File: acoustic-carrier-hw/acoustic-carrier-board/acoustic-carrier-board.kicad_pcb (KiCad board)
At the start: 6 copper layers, 78.8 x 95 mm, 361 parts, among them IC1 ECP5-BGA256, IC1101 MT41K256M16TW-107_P, J1001 BWU.FL-IPEX1, J1002 BWU.FL-IPEX1, J1003 BWU.FL-IPEX1, J1004 BWU.FL-IPEX1, J1005 BWU.FL-IPEX1, J1006 BWU.FL-IPEX1, J1007 8P8C_Shielded, J1008 BWU.FL-IPEX1, J1009 BWU.FL-IPEX1, J1010 BWU.FL-IPEX1, J1201 HR911130A, J202 Conn_02x04_Odd_Even, J701 Conn_01x10_Socket, J702 Conn_01x08_Socket, J801 TYPE-C-31-M-12, J901 Conn_02x08_Odd_Even, Q201 AO3401A, U1001 MS9280, U1002 THS4521IDGK, U1003 DGQ2788AEN-T1-GE4, U1004 LMV321, U1005 TL432DBZ, U1201 KSZ9031RN, U201 TPS2121RUX, U202 TLV62569DBV, U203 TLV62569DBV, U204 TLV62569DBV, U205 TLV62569DBV, U206 OPA376xxDBV, U701 W25Q128JVS, U702 W25Q128JVS, U801 USB3300-EZK, U802 LMV321, Y1201 25MHz, Y401 Crystal Oscillator, Y801 Crystal_GND24_Small

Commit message: [carrier] Layout more or less complete (next) think about adding 6x2 connectors, and add extra pin signals to the connector for testing
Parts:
- removed J1004: BWU.FL-IPEX1, iw-connector:BWU.FL-IPEX1
- removed J202: Conn_02x04_Odd_Even, Connector_PinSocket_2.54mm:PinSocket_2x04_P2.54mm_Horizontal
- removed J702: Conn_01x08_Socket, Connector_PinSocket_2.54mm:PinSocket_1x08_P2.54mm_Horizontal
- removed J901: Conn_02x08_Odd_Even, Connector_PinSocket_2.54mm:PinSocket_2x08_P2.54mm_Horizontal
- removed TP1008: TestPoint, TestPoint:TestPoint_Pad_1.0x1.0mm
- added J201: Conn_02x05_Odd_Even, Connector_PinSocket_2.54mm:PinSocket_2x05_P2.54mm_Horizontal, F.Cu at (115.2, 56.6)
- added J703: Conn_02x05_Odd_Even, Connector_PinSocket_2.54mm:PinSocket_2x05_P2.54mm_Horizontal, F.Cu at (51.3, 103.9)
- added J902: Conn_02x05_Odd_Even, Connector_PinSocket_2.54mm:PinSocket_2x05_P2.54mm_Horizontal, F.Cu at (50.2, 60.9)
- added R1008: 0, Resistor_SMD:R_0603_1608Metric, F.Cu at (66.8, 133.0)
- added R1043: 0, Resistor_SMD:R_0603_1608Metric, F.Cu at (66.8, 138.5)
- C1229, C301, C302, C303, C304, C305, C306, C307, C308, C309, C407, D1201, R1001, R1002, R1003, R1004, R1005, R1025, R1203, R1204, R1206, R1207, R1208, R1209, R1210, R1211, R1212, R1213, R401, R701, R702, R703, RN1201, RN701, RN702, U701, U702: moved to B.Cu
- J1003, J1005: moved to F.Cu
- J701: value Conn_01x10_Socket -> Conn_02x05_Odd_Even; footprint Connector_PinSocket_2.54mm:PinSocket_1x10_P2.54mm_Horizontal -> Connector_PinSocket_2.54mm:PinSocket_2x05_P2.54mm_Horizontal
- R1205: footprint Resistor_SMD:R_0805_2012Metric_Pad1.20x1.40mm_HandSolder -> Resistor_SMD:R_0402_1005Metric; moved to B.Cu
- TP1005: footprint TestPoint:TestPoint_Loop_D1.80mm_Drill1.0mm_Beaded -> TestPoint:TestPoint_THTPad_1.5x1.5mm_Drill0.7mm
- moved TP205 262.9 mm to (-88.4, 99.6)
- moved TP207 262.9 mm to (-89.0, 95.0)
- moved RN701 262.6 mm to (113.2, 107.5), turned to 0 degrees
- moved R701 262.0 mm to (112.7, 116.4), turned to 180 degrees
- moved R702 261.0 mm to (112.7, 115.3), turned to 180 degrees
- moved R703 260.0 mm to (112.7, 114.3), turned to 0 degrees
- moved RN702 258.6 mm to (113.0, 111.5), turned to 180 degrees
- moved TP210 255.9 mm to (-85.2, 105.3)
- moved TP807 255.9 mm to (-93.2, 104.8)
- moved TP801 255.9 mm to (-81.0, 101.5)
- moved TP804 255.9 mm to (-83.7, 94.1)
- moved J701 236.1 mm to (120.1, 112.8), turned to 180 degrees
- moved TP1011 233.0 mm to (-25.4, 94.9)
- moved TP1012 221.8 mm to (-25.8, 100.3), turned to 0 degrees
- moved RN1201 218.5 mm to (77.5, 86.8), turned to 180 degrees
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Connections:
- C1019 pad 1: VCORE_3V3 -> VDDA
- J1007 pad 4: Net-(C1018-Pad1) -> unconnected-(J1007-Pad4)
- J1007 pad 5: Net-(C1017-Pad1) -> unconnected-(J1007-Pad5)
- J1007 pad 7: unconnected-(J1007-Pad7) -> Net-(C1018-Pad1)
- J1007 pad 8: unconnected-(J1007-Pad8) -> Net-(C1017-Pad1)
- J701 pad 10: /FPGA-CONFIG-FLASH/FPGA_RESET -> /FPGA-CONFIG-FLASH/FPGA_CFG1
- J701 pad 2: /FPGA-CONFIG-FLASH/JTAG.TCK -> /FPGA-CONFIG-FLASH/FPGA_RESET
- J701 pad 3: /FPGA-CONFIG-FLASH/JTAG.TDI -> /FPGA-CONFIG-FLASH/JTAG.TCK
- J701 pad 4: /FPGA-CONFIG-FLASH/JTAG.TDO -> /FPGA-CONFIG-FLASH/~{FPGA_INIT}
- J701 pad 5: /FPGA-CONFIG-FLASH/FPGA_CFG0 -> /FPGA-CONFIG-FLASH/JTAG.TDI
- J701 pad 6: /FPGA-CONFIG-FLASH/FPGA_CFG1 -> /FPGA-CONFIG-FLASH/FPGA_DONE
- J701 pad 7: /FPGA-CONFIG-FLASH/FPGA_CFG2 -> /FPGA-CONFIG-FLASH/JTAG.TDO
- J701 pad 8: /FPGA-CONFIG-FLASH/FPGA_DONE -> /FPGA-CONFIG-FLASH/FPGA_CFG2
- J701 pad 9: /FPGA-CONFIG-FLASH/~{FPGA_INIT} -> /FPGA-CONFIG-FLASH/FPGA_CFG0
- RJ1001 pad 1: Net-(J1009-In) -> /ANALOG-FRONTEND/MAG_ADC_AIN-
- RJ1001 pad 2: Net-(J1010-In) -> /ANALOG-FRONTEND/MAG_ADC_AIN+
- RJ1001 pad 3: /ANALOG-FRONTEND/MAG_ADC_AIN- -> Net-(J1009-In)
- RJ1001 pad 4: GND -> Net-(R1039-Pad2)
- RJ1001 pad 5: Net-(R1039-Pad2) -> GND
- RJ1001 pad 6: /ANALOG-FRONTEND/MAG_ADC_AIN+ -> Net-(J1010-In)
- U1003 pad 3: Net-(J1004-In) -> unconnected-(U1003-NO3-Pad3)
- U1003 pad 4: Net-(J1005-In) -> unconnected-(U1003-COM3-Pad4)
- U1003 pad 5: Net-(J1003-In) -> unconnected-(U1003-NC3-Pad5)
- U1003 pad 6: Net-(U1003-IN3-4) -> unconnected-(U1003-IN3-4-Pad6)
- U1004 pad 5: VCORE_3V3 -> VDDA

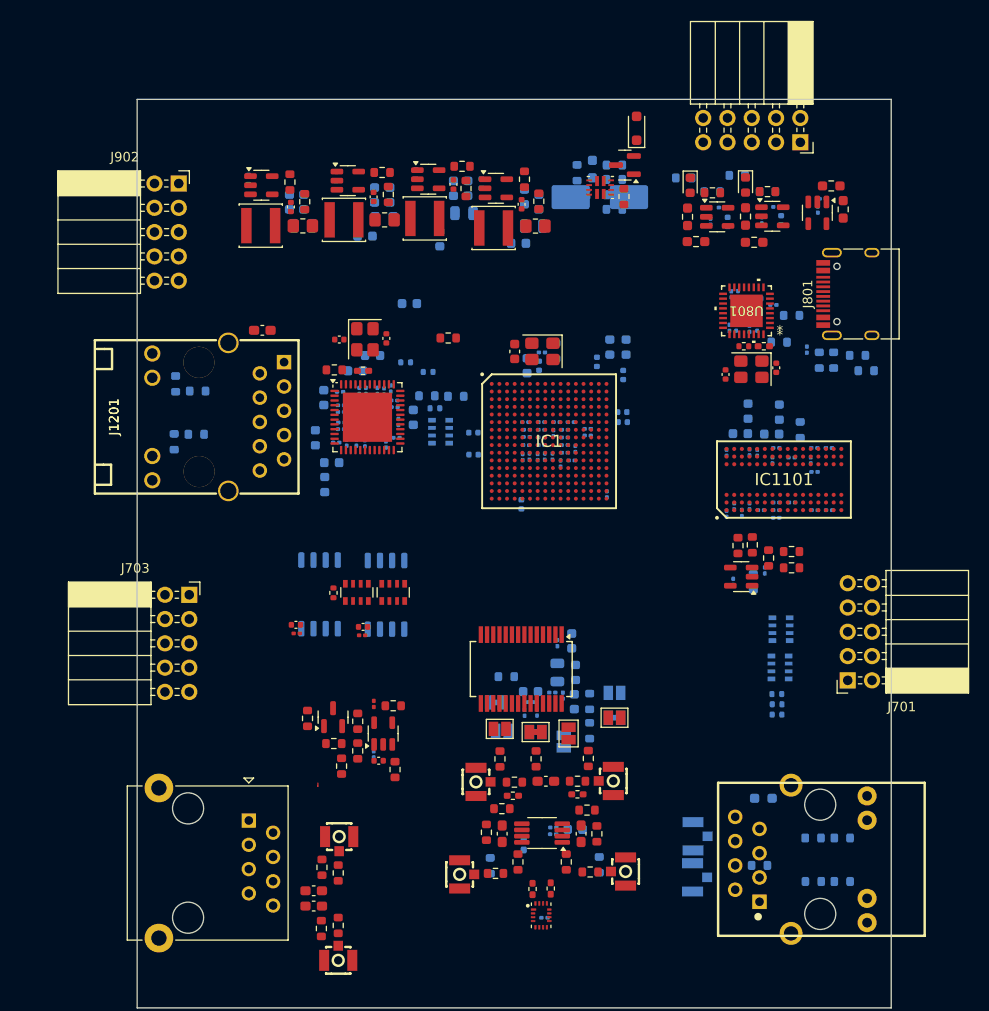
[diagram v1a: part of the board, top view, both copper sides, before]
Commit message: [carrier] Added testpoints to rj45, added 6xx2 connectors (next) start routing the digital section
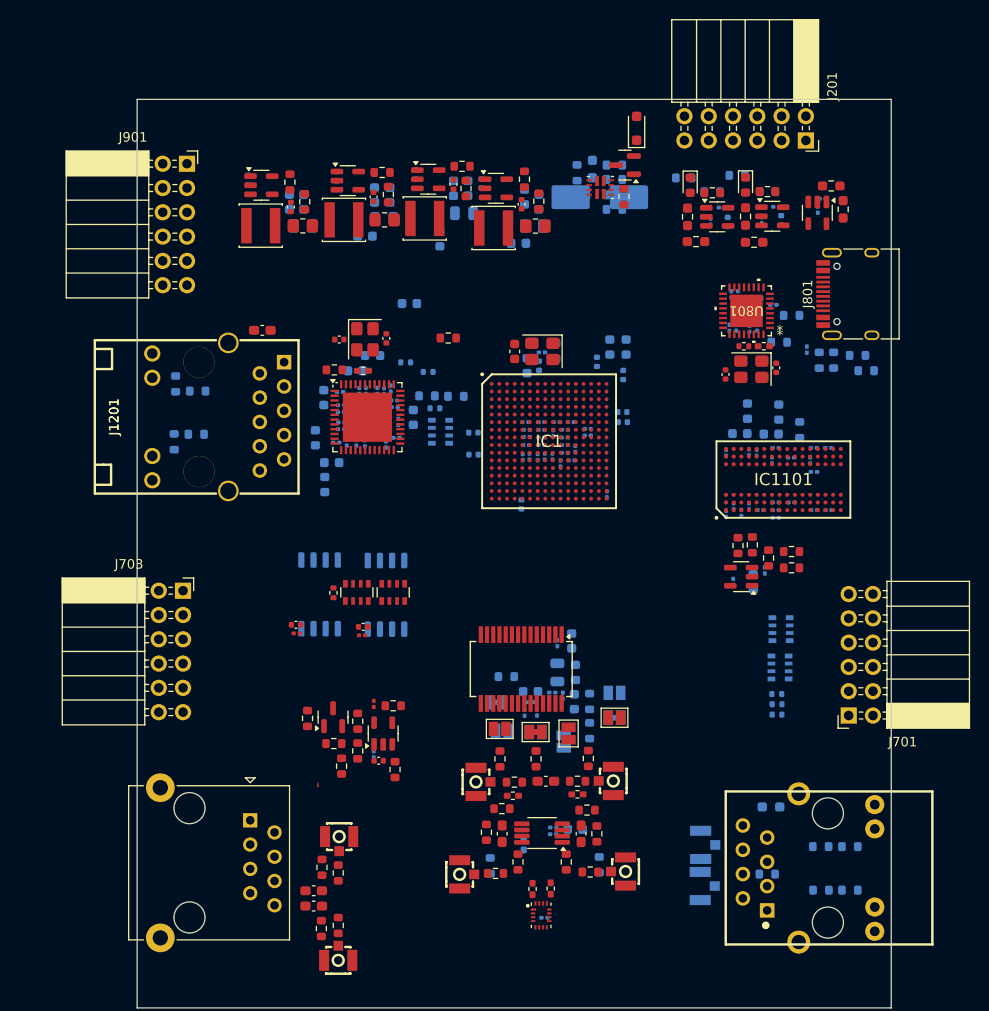
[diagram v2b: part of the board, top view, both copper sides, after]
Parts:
- removed J902: Conn_02x05_Odd_Even, Connector_PinSocket_2.54mm:PinSocket_2x05_P2.54mm_Horizontal
- added J901: Conn_02x06_Odd_Even, Connector_PinSocket_2.54mm:PinSocket_2x06_P2.54mm_Horizontal, F.Cu at (51.0, 58.8)
- J201, J701, J703: value Conn_02x05_Odd_Even -> Conn_02x06_Odd_Even; footprint Connector_PinSocket_2.54mm:PinSocket_2x05_P2.54mm_Horizontal -> Connector_PinSocket_2.54mm:PinSocket_2x06_P2.54mm_Horizontal
- moved J701 3.68 mm to (120.2, 116.5)
- moved J1009 1.21 mm to (105.5, 134.4)
- moved R1001 1.21 mm to (112.1, 126.1)
- moved R1002 1.21 mm to (120.4, 130.2)
- moved R1004 1.21 mm to (120.4, 134.8)
- moved J1010 1.21 mm to (105.5, 130.1)
- moved R1003 1.21 mm to (117.3, 130.2)
- moved R1005 1.21 mm to (117.3, 134.8)
- moved R1039 1.21 mm to (111.7, 133.1)
- moved RJ1001 1.21 mm to (116.1, 132.5)
- moved J703 0.78 mm to (50.6, 103.5)
- moved J201 0.61 mm to (115.8, 56.4)
- moved J1007 0.15 mm to (57.6, 127.5)
- moved C1102 0.06 mm to (111.0, 95.0)
- moved C1105 0.06 mm to (118.1, 88.5)
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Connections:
- J701 pad 1: /FPGA-CONFIG-FLASH/JTAG.TMS -> unconnected-(J701-Pin_1-Pad1)
- J701 pad 10: /FPGA-CONFIG-FLASH/FPGA_CFG1 -> /FPGA-CONFIG-FLASH/JTAG.TDO
- J701 pad 2: /FPGA-CONFIG-FLASH/FPGA_RESET -> unconnected-(J701-Pin_2-Pad2)
- J701 pad 3: /FPGA-CONFIG-FLASH/JTAG.TCK -> /FPGA-CONFIG-FLASH/FPGA_RESET
- J701 pad 4: /FPGA-CONFIG-FLASH/~{FPGA_INIT} -> /FPGA-CONFIG-FLASH/JTAG.TMS
- J701 pad 5: /FPGA-CONFIG-FLASH/JTAG.TDI -> /FPGA-CONFIG-FLASH/~{FPGA_INIT}
- J701 pad 6: /FPGA-CONFIG-FLASH/FPGA_DONE -> /FPGA-CONFIG-FLASH/JTAG.TCK
- J701 pad 7: /FPGA-CONFIG-FLASH/JTAG.TDO -> /FPGA-CONFIG-FLASH/FPGA_DONE
- J701 pad 8: /FPGA-CONFIG-FLASH/FPGA_CFG2 -> /FPGA-CONFIG-FLASH/JTAG.TDI
- J701 pad 9: /FPGA-CONFIG-FLASH/FPGA_CFG0 -> /FPGA-CONFIG-FLASH/FPGA_CFG2
- J703 pad 1: /FPGA-CONFIG-FLASH/QSPI.MCLK -> unconnected-(J703-Pin_1-Pad1)
- J703 pad 10: /FPGA-CONFIG-FLASH/QSPI.D1 -> /FPGA-CONFIG-FLASH/QSPI.CSn
- J703 pad 3: /FPGA-CONFIG-FLASH/QSPI.CSPPIn2 -> unconnected-(J703-Pin_3-Pad3)
- J703 pad 4: unconnected-(J703-Pin_4-Pad4) -> /FPGA-CONFIG-FLASH/QSPI.MCLK
- J703 pad 5: /FPGA-CONFIG-FLASH/QSPI.CSPPIn1 -> unconnected-(J703-Pin_5-Pad5)
- J703 pad 6: /FPGA-CONFIG-FLASH/QSPI.D3 -> /FPGA-CONFIG-FLASH/QSPI.CSPPIn2
- J703 pad 7: /FPGA-CONFIG-FLASH/QSPI.CSn -> /FPGA-CONFIG-FLASH/QSPI.D3
- J703 pad 8: /FPGA-CONFIG-FLASH/QSPI.D2 -> /FPGA-CONFIG-FLASH/QSPI.CSPPIn1
- J703 pad 9: /FPGA-CONFIG-FLASH/QSPI.D0 -> /FPGA-CONFIG-FLASH/QSPI.D2

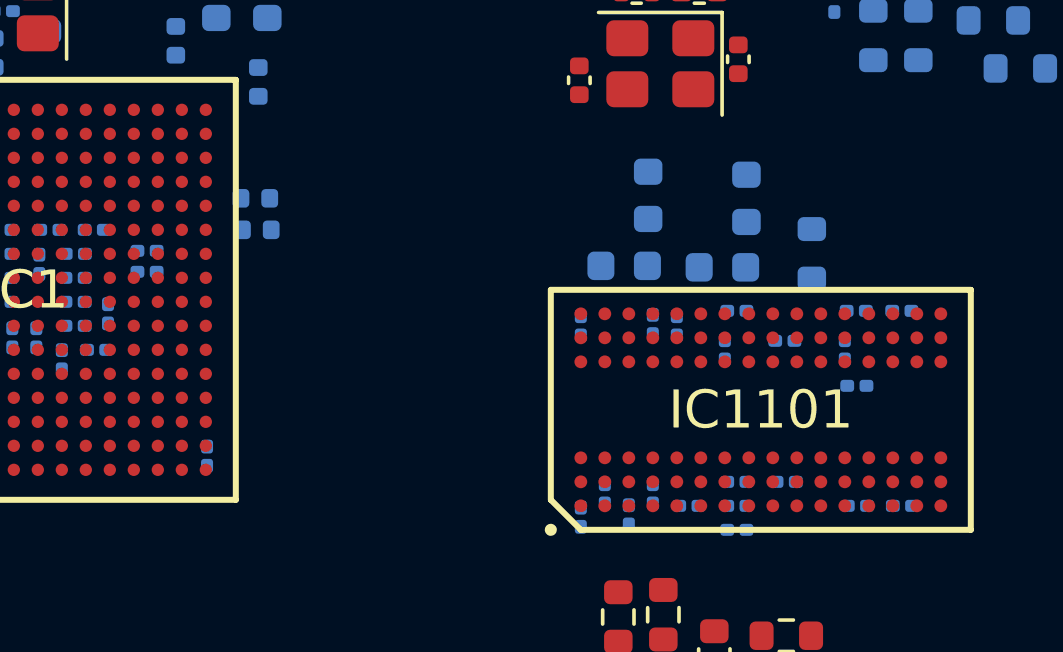
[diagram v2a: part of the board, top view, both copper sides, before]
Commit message: [carrier] trying horizontal layout
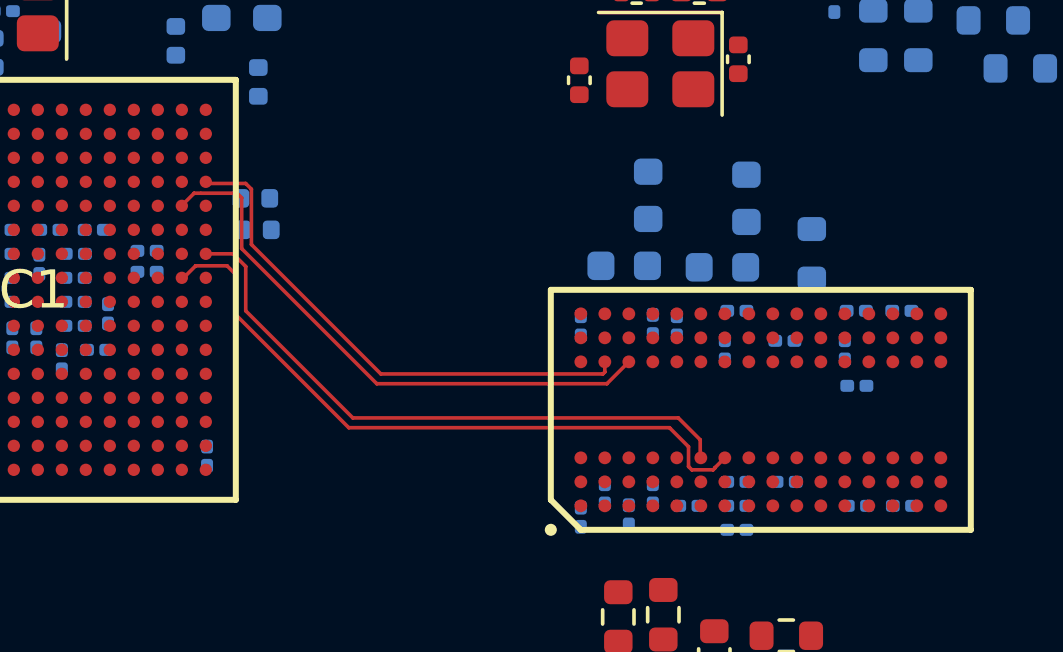
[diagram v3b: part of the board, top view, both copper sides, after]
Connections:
- net /DDR3/DDR3.CK renamed /DDR3/DDR3.CK+
- net /DDR3/DDR3.CK# renamed /DDR3/DDR3.CK-
- IC1 pad B15: /DDR3/DDR3.DQ1 -> /DDR3/DDR3.DQ9
- IC1 pad B16: /DDR3/DDR3.DQ0 -> /DDR3/DDR3.DQ11
- IC1 pad C14: /DDR3/DDR3.DQ2 -> /DDR3/DDR3.DQ12
- IC1 pad C15: /DDR3/DDR3.DQ5 -> /DDR3/DDR3.DQ10
- IC1 pad C16: /DDR3/DDR3.DQ4 -> /DDR3/DDR3.DQ14
- IC1 pad D14: /DDR3/DDR3.DQ3 -> /DDR3/DDR3.DQ8
- IC1 pad D16: /DDR3/DDR3.LDQS -> /DDR3/DDR3.UDQS+
- IC1 pad E14: /DDR3/DDR3.DQ6 -> /DDR3/DDR3.DQ15
- IC1 pad E15: /DDR3/DDR3.LDQS# -> /DDR3/DDR3.UDQS-
- IC1 pad E16: /DDR3/DDR3.LDM -> /DDR3/DDR3.UDM
- IC1 pad F15: /DDR3/DDR3.DQ7 -> /DDR3/DDR3.DQ13
- IC1 pad F16: /DDR3/DDR3.DQ8 -> /DDR3/DDR3.LDM
- IC1 pad G15: /DDR3/DDR3.DQ9 -> /DDR3/DDR3.DQ7
- IC1 pad G16: /DDR3/DDR3.UDQS -> /DDR3/DDR3.LDQS+
- IC1 pad H14: /DDR3/DDR3.DQ10 -> /DDR3/DDR3.DQ6
- IC1 pad H15: /DDR3/DDR3.UDQS# -> /DDR3/DDR3.LDQS-
- IC1 pad J14: /DDR3/DDR3.DQ11 -> /DDR3/DDR3.DQ5
- IC1 pad J15: /DDR3/DDR3.DQ14 -> /DDR3/DDR3.DQ2
- IC1 pad J16: /DDR3/DDR3.DQ13 -> /DDR3/DDR3.DQ3
- IC1 pad K14: /DDR3/DDR3.DQ12 -> /DDR3/DDR3.DQ4
- IC1 pad K15: /DDR3/DDR3.UDM -> /DDR3/DDR3.DQ0
- IC1 pad K16: /DDR3/DDR3.DQ15 -> /DDR3/DDR3.DQ1
- IC1101 pad B7: /DDR3/DDR3.UDQS# -> /DDR3/DDR3.UDQS+
- IC1101 pad C7: /DDR3/DDR3.UDQS -> /DDR3/DDR3.UDQS-
- IC1101 pad F3: /DDR3/DDR3.LDQS -> /DDR3/DDR3.LDQS+
- IC1101 pad G3: /DDR3/DDR3.LDQS# -> /DDR3/DDR3.LDQS-
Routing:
- net /DDR3/DDR3.LDQS-: track 0.00 -> 22.4 mm
- net /DDR3/DDR3.LDQS+: track 0.00 -> 20.5 mm
- net /DDR3/DDR3.UDQS-: track 0.00 -> 19.0 mm
- net /DDR3/DDR3.UDQS+: track 0.00 -> 17.5 mm
